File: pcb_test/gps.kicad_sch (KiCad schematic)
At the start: 0 parts

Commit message: Ajout GPS, retrait radio, clean up schemas
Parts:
- added C46: 1u, symbol Device:C
- added C47: 0.1u, symbol Device:C
- added R43, R44, R45, R46: 0R, symbol Device:R
- added R53, R54: 10k, symbol Device:R
- added U12: SAM-M8Q, RF_GPS:ublox_SAM-M8Q, symbol RF_GPS:SAM-M8Q
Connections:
- new net: R45.1, U12.9 (SDA)
- new net: R46.1, U12.12 (SCL)
- new net +3.3V: C46.1, C47.1, R53.1, R54.1, U12.17 (VCC), U12.2 (VCC_IO)
- new net GND: C46.2, C47.2, U12.1 (GND), U12.10 (GND), U12.11 (GND), U12.15 (GND), U12.16 (GND), U12.20 (GND), U12.4 (GND), U12.5 (GND), U12.6 (GND)
- new net GPS_RX: R43.1, R43.2, U12.14 (RXD)
- new net GPS_SCL: R46.2, R54.2
- new net GPS_SDA: R45.2, R53.2
- new net GPS_TX: R44.1, R44.2, U12.13 (TXD)
- new net RESET_n: U12.18 (~{RESET})
- new net SAFEBOOT_n: U12.8 (~{SAFEBOOT})
- no-connect marks 0 -> 3
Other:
- note added: "Antenna is integrated in the module"
- note added: "GPS module"

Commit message: Ajout testpoints
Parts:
- added TP57, TP58, TP59, TP60, TP61, TP62, TP63, TP64: TestPoint, symbol Connector:TestPoint
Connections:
- net GND: now also TP60.1, TP62.1
- net GPS_RX: now also TP61.1
- net GPS_SCL: now also TP57.1
- net GPS_SDA: now also TP58.1
- net GPS_TX: now also TP59.1
- net RESET_n: now also TP64.1
- net SAFEBOOT_n: now also TP63.1

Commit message: refait alimentation, changement MCU, separation schema eMMC/octospi, reajout RF
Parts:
- R43, R44, R45, R46, R53, R54: symbol Device:R -> Device:R_US
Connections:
- net GPS_RX: no longer R43.1, U12.14 (RXD)
- net GPS_TX: no longer R44.1, U12.13 (TXD)
- net RCC32_CLK_SRC: now reaches U12.7 (TIMEPULSE)
- new net: R44.1, U12.13 (TXD)
- new net: R43.1, U12.14 (RXD)
- no-connect marks 3 -> 2
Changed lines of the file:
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@@
 	(paper "A4")
 	(rectangle
-		(start 12.7 24.13)
+		(start 12.7 12.7)
 		(end 114.3 88.9)
 		(stroke
@@
 	)
 	(junction
-		(at 73.66 44.45)
-		(diameter 0)
-		(color 0 0 0 0)
-	)
-	(junction
 		(at 91.44 31.75)
-		(diameter 0)
-		(color 0 0 0 0)
-	)
-	(junction
-		(at 66.04 44.45)
-		(diameter 0)
-		(color 0 0 0 0)
-	)
-	(junction
-		(at 72.39 46.99)
 		(diameter 0)
 		(color 0 0 0 0)
@@
 	)
 	(junction
-		(at 80.01 46.99)
-		(diameter 0)
-		(color 0 0 0 0)
-	)
-	(junction
 		(at 26.67 33.02)
 		(diameter 0)
@@
 		(at 54.61 36.83)
 	)
-	(no_connect
-		(at 39.37 49.53)
-	)
 	(wire
 		(pts
@@
 	(wire
 		(pts
+			(xy 35.56 49.53) (xy 39.37 49.53)
+		)
+		(stroke
+			(width 0)
+			(type default)
+		)
+	)
+	(wire
+		(pts
 			(xy 92.71 54.61) (xy 100.33 54.61)
 		)
@@
 	(wire
 		(pts
-			(xy 72.39 46.99) (xy 80.01 46.99)
-		)
-		(stroke
-			(width 0)
-			(type default)
-		)
-	)
-	(wire
-		(pts
 			(xy 91.44 30.48) (xy 91.44 31.75)
 		)
@@
 		(pts
 			(xy 52.07 36.83) (xy 52.07 35.56)
-		)
-		(stroke
-			(width 0)
-			(type default)
-		)
-	)
-	(wire
-		(pts
-			(xy 66.04 44.45) (xy 73.66 44.45)
 		)
 		(stroke
@@
 		(property "Intersheetrefs" "${INTERSHEET_REFS}"
 			(at 104.14 78.1569 90)
+			(hide yes)
+			(show_name no)
+			(do_not_autoplace no)
+			(effects
+				(font
+					(size 1.27 1.27)
+				)
+				(justify right)
+			)
+		)
+	)
+	(global_label "RCC32_CLK_SRC"
+		(shape input)
+		(at 35.56 49.53 180)
+		(fields_autoplaced yes)
+		(effects
+			(font
+				(size 1.27 1.27)
+			)
+			(justify right)
+		)
+		(property "Intersheetrefs" "${INTERSHEET_REFS}"
+			(at 17.093 49.53 0)
 			(hide yes)
 			(show_name no)
@@
 	)
 	(symbol
-		(lib_id "Device:R")
+		(lib_id "Device:R_US")
 		(at 82.55 52.07 90)
 		(unit 1)
@@
 		)
 		(property "Footprint" ""
-			(at 82.55 53.848 90)
+			(at 82.804 51.054 90)
 			(hide yes)
 			(show_name no)
@@
 			)
 		)
-		(property "Description" "Resistor"
+		(property "Description" "Resistor, US symbol"
 			(at 82.55 52.07 0)
 			(hide yes)
@@
 	)
 	(symbol
-		(lib_id "Device:R")
+		(lib_id "Device:R_US")
 		(at 76.2 46.99 90)
 		(unit 1)
@@
 		)
 		(property "Footprint" ""
-			(at 76.2 48.768 90)
+			(at 76.454 45.974 90)
 			(hide yes)
 			(show_name no)
@@
 			)
 		)
-		(property "Description" "Resistor"
+		(property "Description" "Resistor, US symbol"
 			(at 76.2 46.99 0)
 			(hide yes)
@@
 	)
 	(symbol
-		(lib_id "Device:R")
+		(lib_id "Device:R_US")
 		(at 100.33 36.83 0)
 		(unit 1)
@@
 		)
 		(property "Footprint" ""
-			(at 98.552 36.83 90)
+			(at 101.346 37.084 90)
 			(hide yes)
 			(show_name no)
@@
 			)
 		)
-		(property "Description" "Resistor"
+		(property "Description" "Resistor, US symbol"
 			(at 100.33 36.83 0)
 			(hide yes)
@@
 	)
 	(symbol
-		(lib_id "Device:R")
+		(lib_id "Device:R_US")
 		(at 88.9 54.61 90)
 		(unit 1)
@@
 		)
 		(property "Footprint" ""
-			(at 88.9 56.388 90)
+			(at 89.154 53.594 90)
 			(hide yes)
 			(show_name no)
@@
 			)
 		)
-		(property "Description" "Resistor"
+		(property "Description" "Resistor, US symbol"
 			(at 88.9 54.61 0)
 			(hide yes)
@@
 	)
 	(symbol
-		(lib_id "Device:R")
+		(lib_id "Device:R_US")
 		(at 91.44 36.83 0)
 		(unit 1)
@@
 		)
 		(property "Footprint" ""
-			(at 89.662 36.83 90)
+			(at 92.456 37.084 90)
 			(hide yes)
 			(show_name no)
@@
 			)
 		)
-		(property "Description" "Resistor"
+		(property "Description" "Resistor, US symbol"
 			(at 91.44 36.83 0)
 			(hide yes)
@@
 	)
 	(symbol
-		(lib_id "Device:R")
+		(lib_id "Device:R_US")
 		(at 69.85 44.45 90)
 		(unit 1)
@@
 		)
 		(property "Footprint" ""
-			(at 69.85 46.228 90)
+			(at 70.104 43.434 90)
 			(hide yes)
 			(show_name no)
@@
 			)
 		)
-		(property "Description" "Resistor"
+		(property "Description" "Resistor, US symbol"
 			(at 69.85 44.45 0)
 			(hide yes)

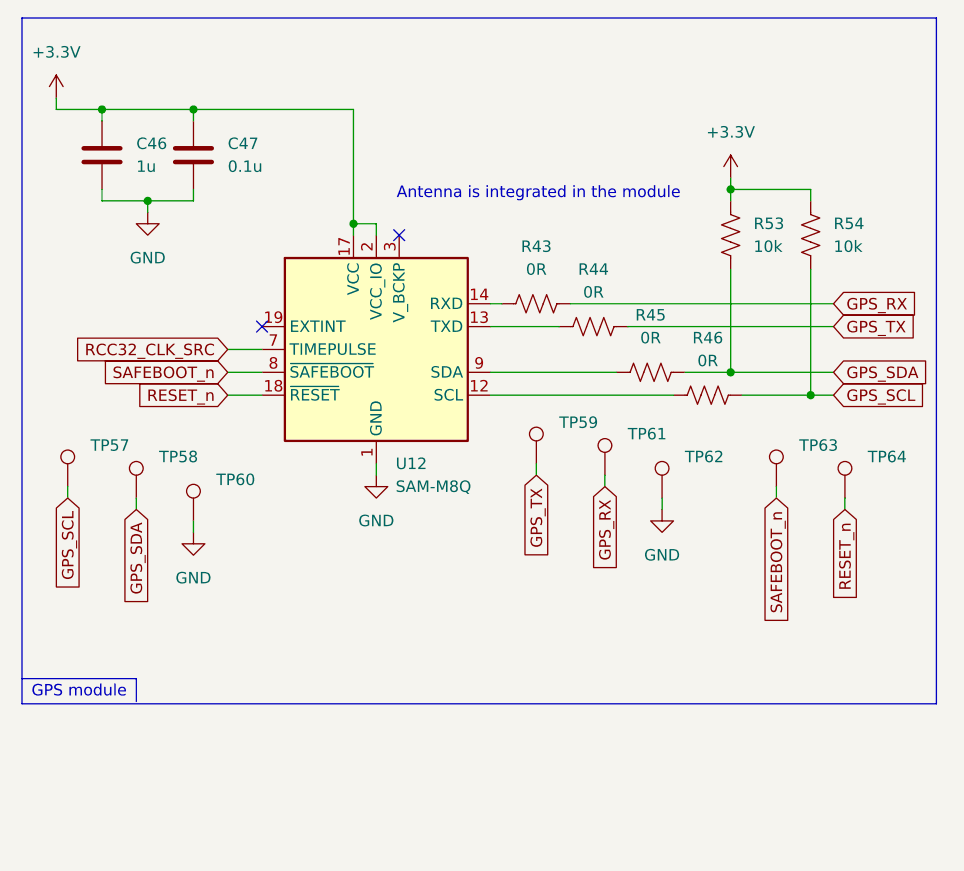
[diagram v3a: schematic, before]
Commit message: alimentation finale. Retouches testpoints et condo decouplage, finalisation requis, ajout sheet finale.
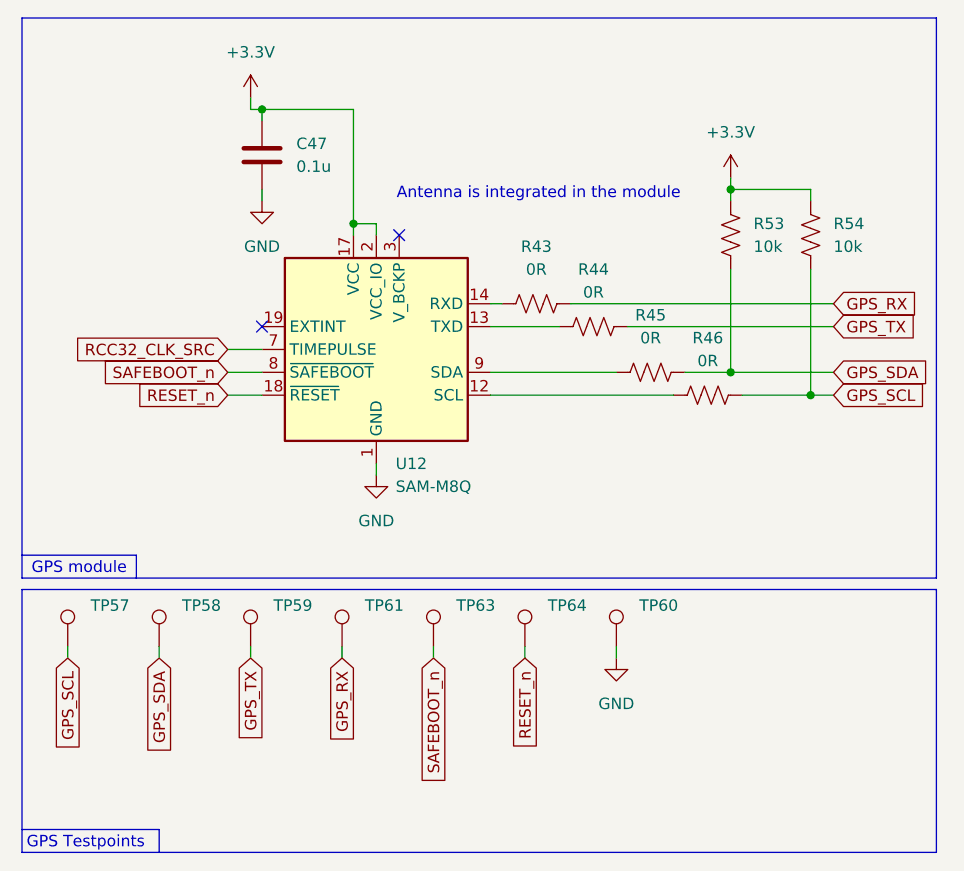
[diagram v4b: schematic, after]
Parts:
- removed C46: 1u, symbol Device:C
- removed TP62: TestPoint, symbol Connector:TestPoint
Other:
- note added: "GPS Testpoints"
- moved on the sheet: C47, TP57, TP58, TP59, TP60, TP61, TP63, TP64
